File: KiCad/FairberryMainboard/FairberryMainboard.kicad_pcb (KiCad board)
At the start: 2 copper layers, 39.7 x 19.3 mm, 19 parts, among them J1 USB_Header, J2 Conn_02x03_Odd_Even, J3 Conn_02x02_Odd_Even, J4 Conn_01x02, U1 ATmega32U4-MU, U2 BBQ10KBD, Y1 Crystal_GND24

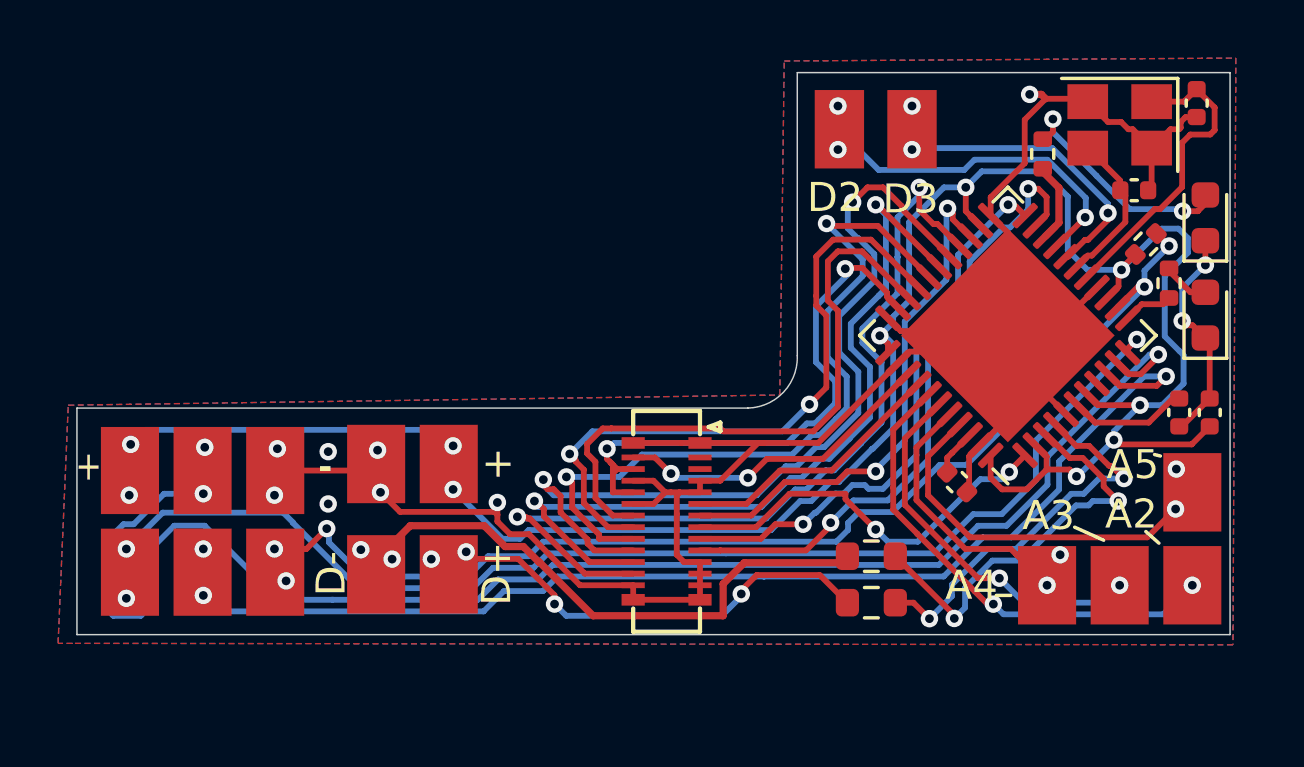
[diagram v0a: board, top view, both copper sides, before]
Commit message: Split backlight into two zones, removed status LEDs, reduced y size by 1mm
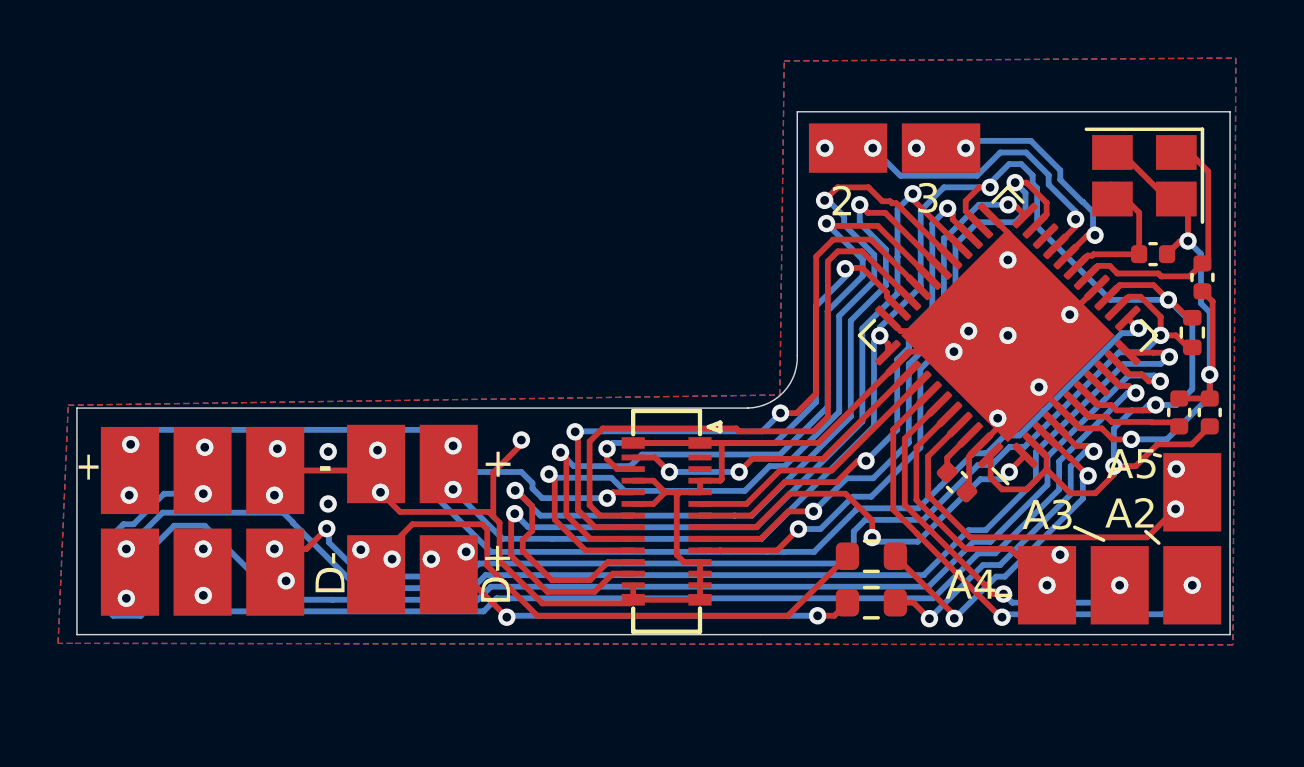
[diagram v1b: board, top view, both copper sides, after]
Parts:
- removed D1: LED Blue, LED_SMD:LED_0603_1608Metric
- removed D2: LED Yellow, LED_SMD:LED_0603_1608Metric
- removed R4: 470, Resistor_SMD:R_0402_1005Metric
- removed R5: 680, Resistor_SMD:R_0402_1005Metric
- ?: renamed from J4; footprint Fairberry:TestPoint_Pad_1x2_2.0x3.0mm -> Fairberry:TestPoint_Pad_1x2_2.0x3.0mm_Rotated
- moved C4 6.00 mm to (190.5, 84.3)
- moved R1 3.44 mm to (190.2, 86.2), turned to -90 degrees
- moved C5 2.29 mm to (188.8, 83.5)
- moved Y1 1.95 mm to (188.5, 80.8)
- moved ? 0.72 mm to (178.3, 79.8)
- turned C1 to 90 degrees
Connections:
- U1 pad 12: Net-(R4-Pad1) -> Net-(U1-Pad12)
- U1 pad 20: Net-(R5-Pad1) -> unconnected-(U1-Pad20)
- U2 pad 24: Net-(U1-Pad32) -> Net-(U1-Pad12)
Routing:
- net Net-(U1-Pad12): track 0.00 -> 36.7 mm, vias 0 -> 2
- net Net-(D2-Pad2): track 7.87 -> 0.00 mm, vias 2 -> 0
- net GND: track 88.7 -> 92.8 mm, vias 10 -> 17
- net Net-(U1-Pad32): track 19.8 -> 16.8 mm
- net Net-(U1-Pad28): track 29.3 -> 32.1 mm
- net Net-(R5-Pad1): track 2.64 -> 0.00 mm
- net Net-(J2-Pad3): track 41.2 -> 38.9 mm
- net /USB_UC_D-: track 14.3 -> 12.0 mm
- net Net-(J4-Pad2): track 11.6 -> 9.52 mm
- net /USB_UC_D+: track 13.5 -> 11.7 mm
- net Net-(R4-Pad1): track 1.71 -> 0.00 mm
- net Net-(D1-Pad2): track 1.64 -> 0.00 mm
- net Net-(J2-Pad1): track 43.1 -> 44.6 mm
- net Net-(J3-Pad2): track 11.9 -> 10.4 mm
- net Net-(C4-Pad1): track 10.8 -> 9.36 mm
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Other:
- board size 39.7 x 19.3 mm -> 39.7 x 18 mm
- board text added: "2"
- board text added: "24.01.2024 Fairberry v0.3.0 ©Dakkaron, 2024"
- board text added: "3"
- board text removed: "10.07.2022 Fairberry v0.2.0 ©Dakkaron, 2022"
- board text removed: "D2"
- board text removed: "D3"

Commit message: Finished v0.3.0
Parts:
- ?: renamed from J3; footprint Fairberry:TestPoint_Pad_1+3_2.0x3.0mm_slim -> Fairberry:TestPoint_Pad_2+2_Z_2.0x2.0mm
- moved J4 26.9 mm to (155.6, 94.2), turned to 90 degrees
- moved J2 4.63 mm to (158.2, 90.9)
- moved J1 4.35 mm to (166.4, 90.9)
- moved Y1 3.26 mm to (189.1, 84.0), turned to 0 degrees
- moved C5 2.30 mm to (186.5, 83.3), turned to -90 degrees
- moved R3 1.96 mm to (178.4, 95.8)
- moved U1 1.92 mm to (183.5, 88.2)
- moved C4 1.92 mm to (190.2, 86.2), turned to 0 degrees
- moved U2 1.85 mm to (173.9, 92.7)
- moved C3 1.72 mm to (181.1, 92.8)
- moved R1 1.57 mm to (189.9, 87.8)
- moved R2 1.45 mm to (178.4, 94.2)
- moved C1 1.40 mm to (189.8, 90.3)
- moved C2 1.40 mm to (190.8, 90.3)
- moved ? 0.70 mm to (187.7, 92.5)
- gave numbers to parts that had none: 1
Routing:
- net Net-(J4-Pad2): track 9.52 -> 37.7 mm
- net Net-(J4-Pad1): track 11.9 -> 38.8 mm
- net Net-(J2-Pad4): track 53.4 -> 32.6 mm, vias 3 -> 2
- net Net-(U1-Pad26): track 31.2 -> 15.8 mm
- net Net-(U1-Pad28): track 32.1 -> 17.5 mm
- net GND: track 92.8 -> 78.6 mm, vias 17 -> 6
- net VCC: track 79.0 -> 67.3 mm
- net Net-(U1-Pad27): track 30.2 -> 18.9 mm
- net Net-(U1-Pad12): track 36.7 -> 25.9 mm, vias 2 -> 4
- net Net-(U1-Pad29): track 26.7 -> 18.3 mm
- net Net-(J2-Pad3): track 38.9 -> 31.5 mm
- net Net-(J2-Pad5): track 40.6 -> 33.5 mm
- net /USB_Plug_D-: track 20.6 -> 13.8 mm
- net Net-(U1-Pad30): track 22.9 -> 16.3 mm
- net Net-(J2-Pad1): track 44.6 -> 38.3 mm
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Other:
- board size 39.7 x 18 mm -> 37.3 x 14.7 mm
- board text added: "14.02.2024 Fairberry v0.3.0 ©Dakkaron, 2024"
- board text removed: "24.01.2024 Fairberry v0.3.0 ©Dakkaron, 2024"
